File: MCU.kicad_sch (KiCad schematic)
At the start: 19 parts, among them U3 STM32F072CBTx

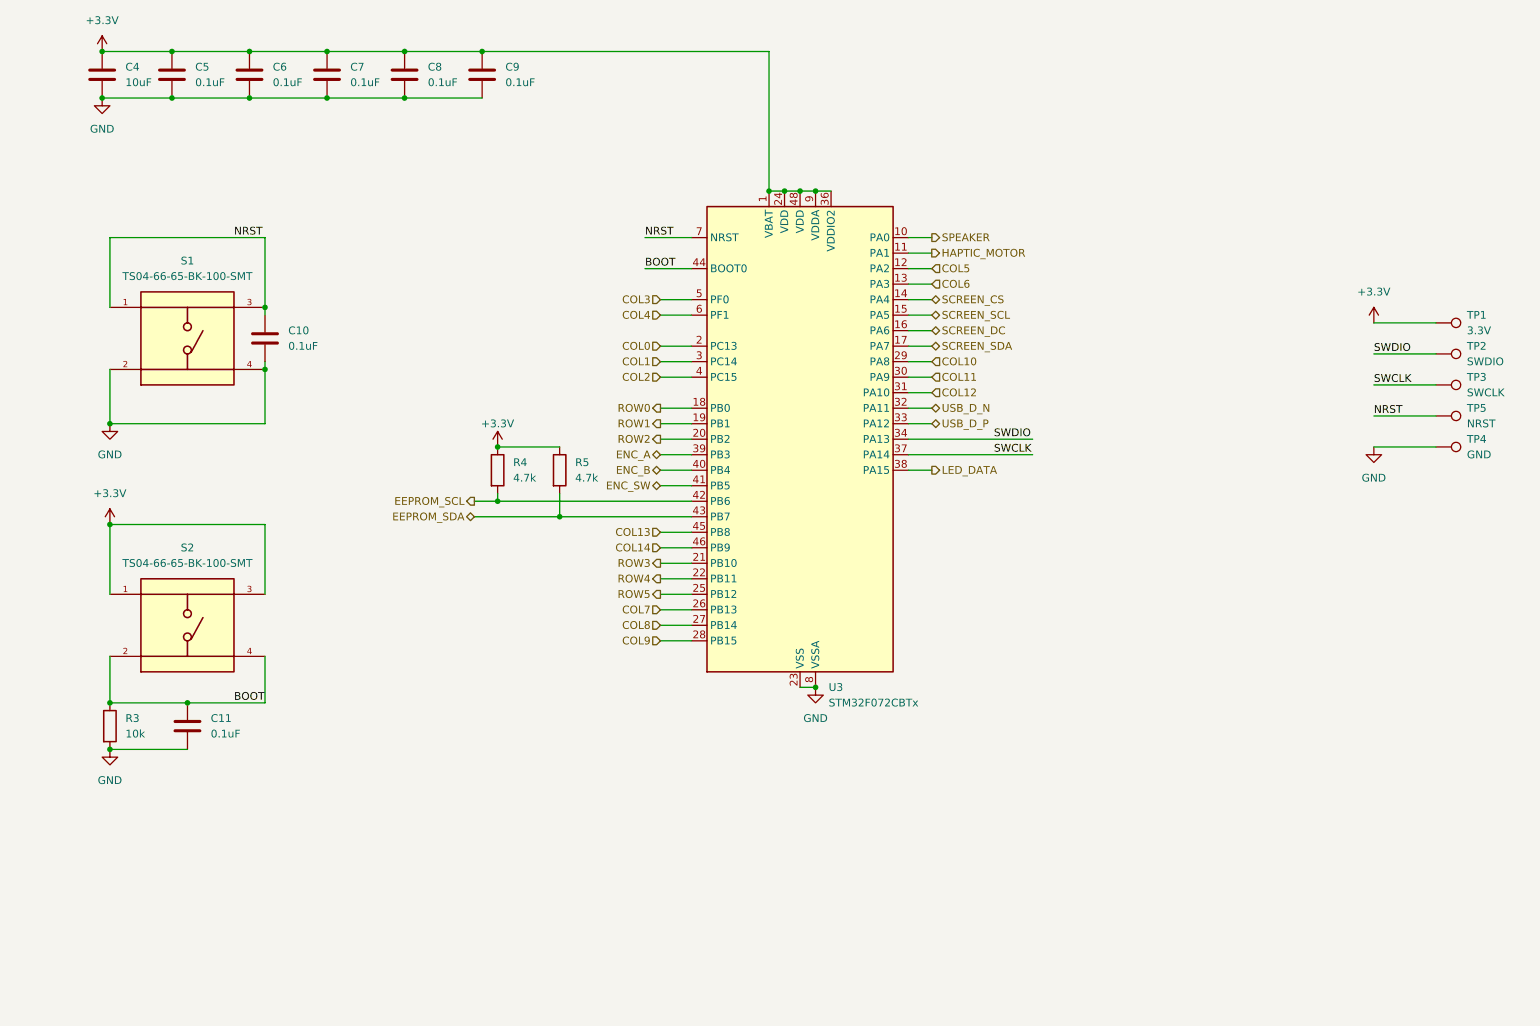
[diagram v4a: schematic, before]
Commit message: added mcu documentation, also updated boot & reset circuitry to follow acheron recommended guide
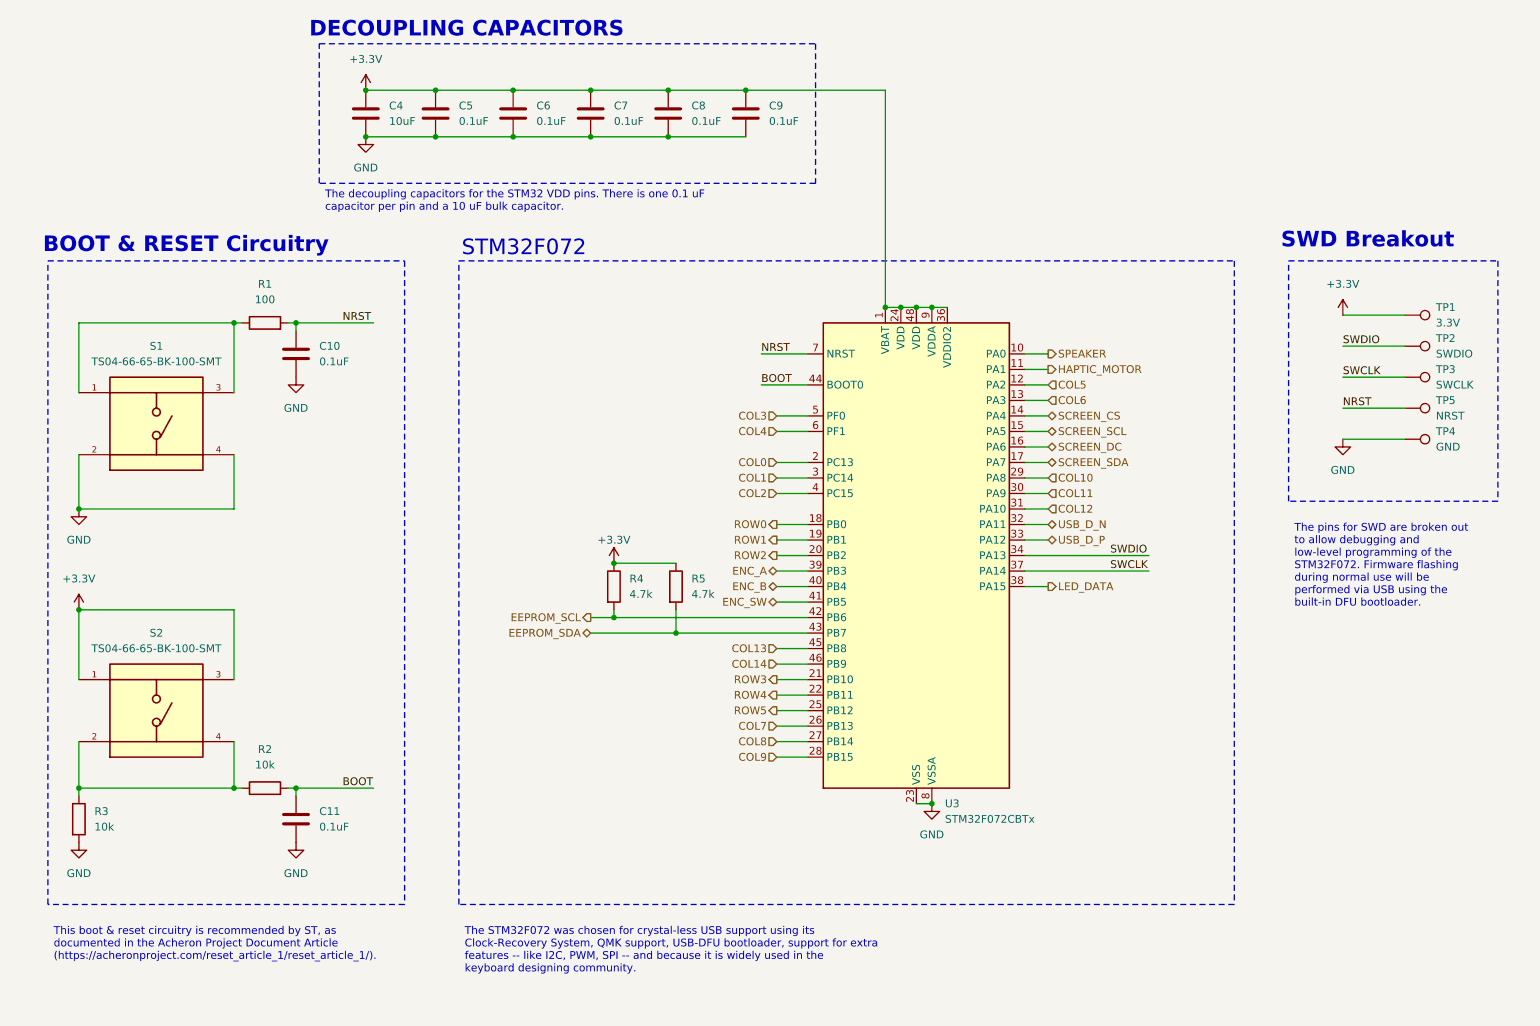
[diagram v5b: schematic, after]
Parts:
- added R1: 100, symbol Device:R
- added R2: 10k, symbol Device:R
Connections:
- net BOOT: now also R2.2; no longer R3.1, S2.2, S2.4
- net NRST: now also R1.2; no longer S1.1, S1.3
- new net: R1.1, S1.1, S1.3
- new net: R2.1, R3.1, S2.2, S2.4
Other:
- note added: "BOOT & RESET Circuitry"
- note added: "DECOUPLING CAPACITORS"
- note added: "STM32F072"
- note added: "SWD Breakout"
- moved on the sheet: C10, C11, C4, C5, C6, C7, C8, C9, R3, R4, R5, S1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
